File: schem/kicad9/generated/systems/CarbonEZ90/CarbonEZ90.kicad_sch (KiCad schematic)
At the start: 0 parts

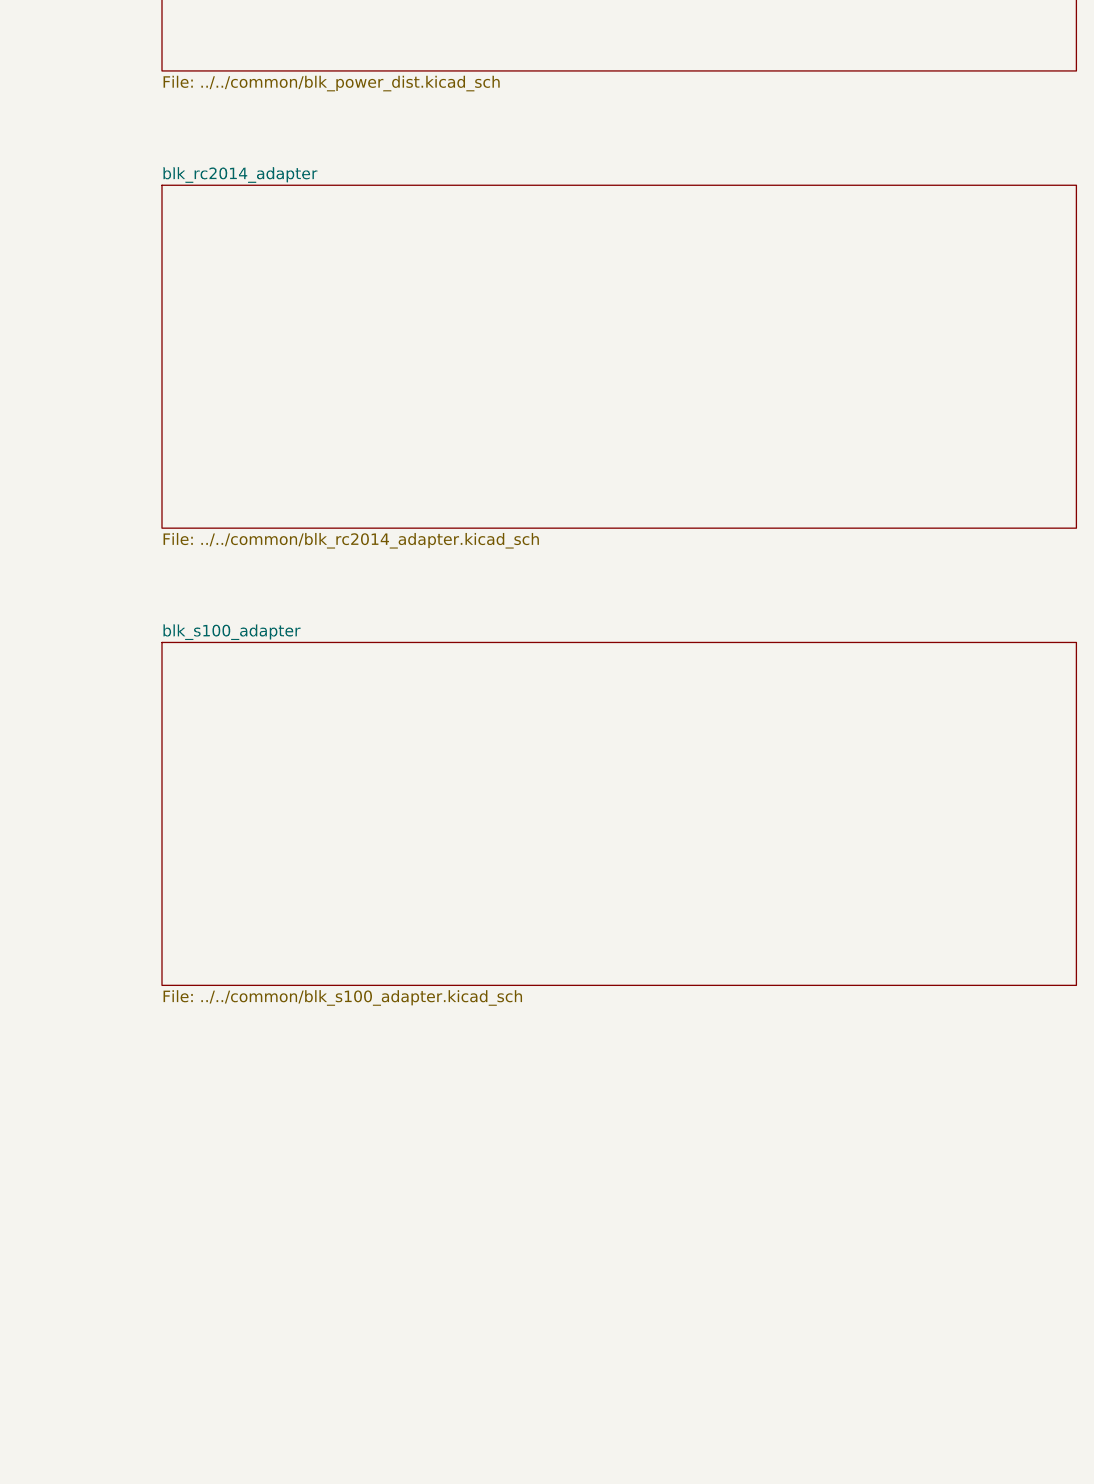
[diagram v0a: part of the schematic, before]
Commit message: kicad: add carbon block symbol library + docs + regen scripts
Detailed description:
- What was implemented: added schem/kicad9/libs/carbon_blocks.kicad_sym placeholder symbols, schem/kicad9/docs/USAGE.md, and scripts/gen_kicad.ps1 plus scripts/gen_kicad.sh; generator now embeds and uses carbon_blocks symbols in generated common block sheets and adds a JTAG/UART common block to system tops.
- Why it exists: keeps the generated hierarchy self-contained and makes regeneration repeatable while reserving a clear path to later map blocks to real parts.
- Architectural assumptions: generator overwrites only schem/kicad9/generated/; carbon_blocks symbols are placeholders (no pin-level mapping in v1); common blocks are represented as simple symbols inside common subsheets.
- How to run it: scripts/gen_kicad.ps1 or scripts/gen_kicad.sh (or python tools/kicadgen/src/kicadgen.py).
- What is NOT implemented yet: automatic mapping to specific 74ACT parts and real footprints, detailed per-net wiring between blocks, and deeper parsing of hdl/spec YAML beyond the mapping specs.
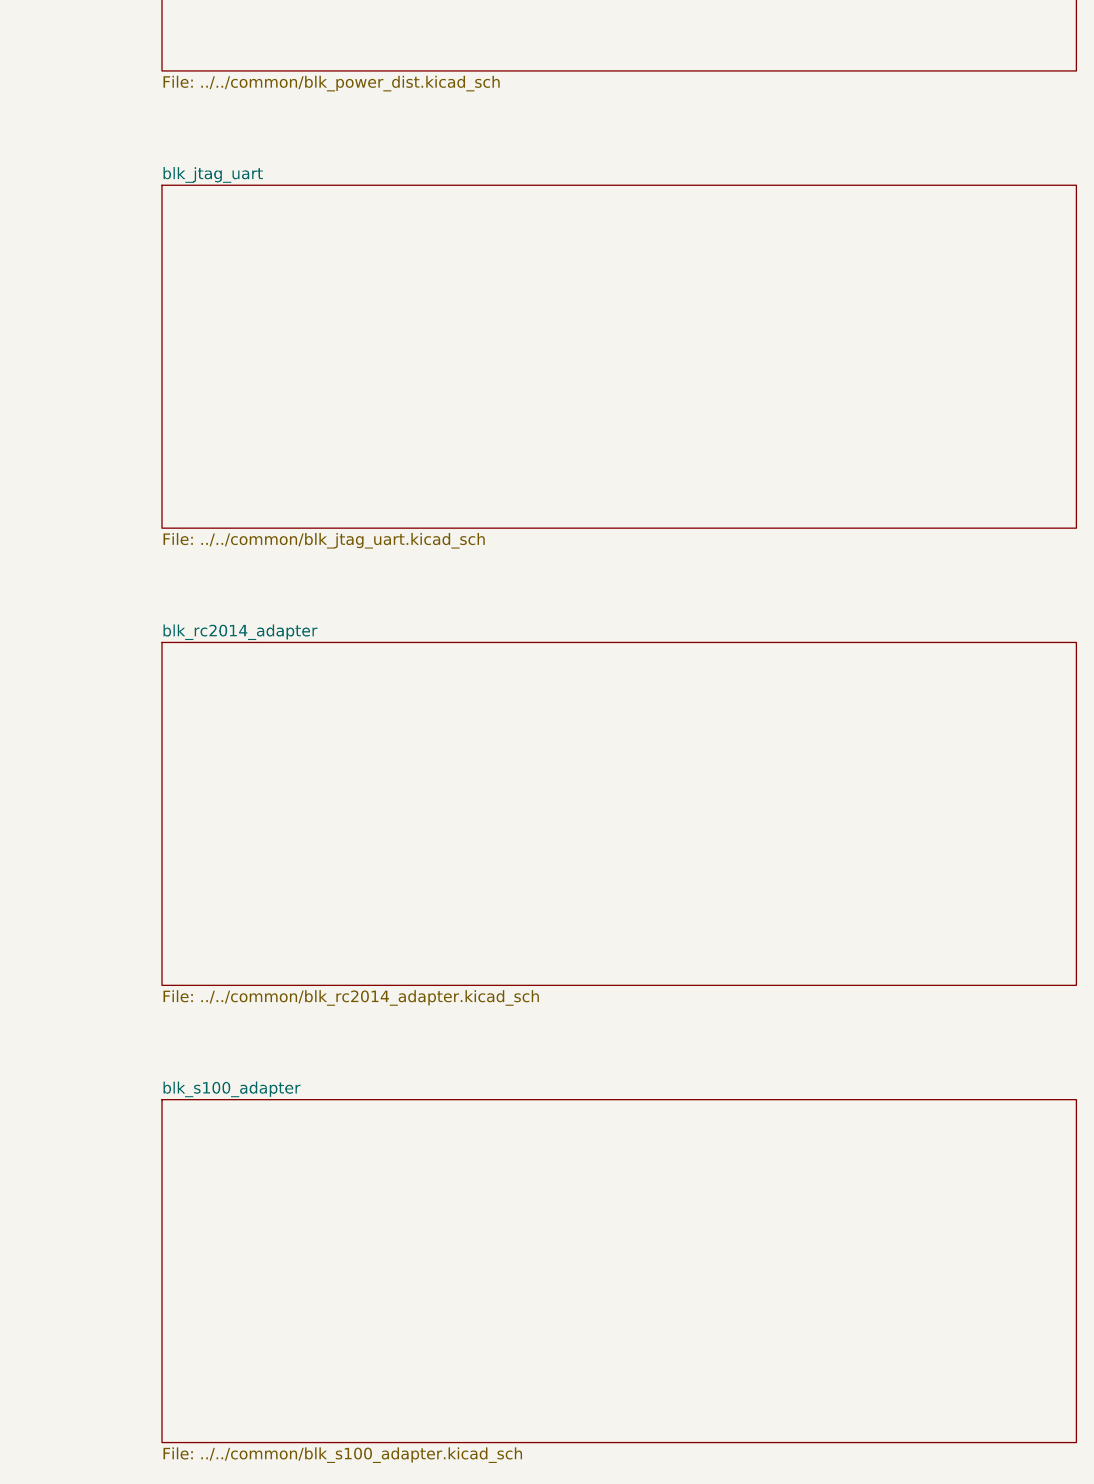
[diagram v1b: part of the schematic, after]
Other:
- added sheet blk_jtag_uart (../../common/blk_jtag_uart.kicad_sch)
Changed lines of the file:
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@@
 		(property
 			"Sheetname"
-			"blk_rc2014_adapter"
+			"blk_jtag_uart"
 			(at
 				139.7
@@
 		(property
 			"Sheetfile"
-			"../../common/blk_rc2014_adapter.kicad_sch"
+			"../../common/blk_jtag_uart.kicad_sch"
 			(at
 				139.7
@@
 		(property
 			"Sheetname"
-			"blk_s100_adapter"
+			"blk_rc2014_adapter"
 			(at
 				139.7
@@
 		(property
 			"Sheetfile"
-			"../../common/blk_s100_adapter.kicad_sch"
+			"../../common/blk_rc2014_adapter.kicad_sch"
 			(at
 				139.7
@@
 				)
 			)
+		)
+	)
+	(sheet
+		(at 139.7 345.44)
+		(size 101.6 38.1)
+		(exclude_from_sim no)
+		(in_bom yes)
+		(on_board yes)
+		(dnp no)
+		(stroke
+			(width 0)
+			(type solid)
+		)
+		(fill
+			(color
+				0
+				0
+				0
+				0
+			)
+		)
+		(property
+			"Sheetname"
+			"blk_s100_adapter"
+			(at
+				139.7
+				344.17
+				0
+			)
+			(effects
+				(font
+					(size 1.27 1.27)
+				)
+				(justify left)
+			)
+		)
+		(property
+			"Sheetfile"
+			"../../common/blk_s100_adapter.kicad_sch"
+			(at
+				139.7
+				384.81
+				0
+			)
+			(effects
+				(font
+					(size 1.27 1.27)
+				)
+				(justify left)
+			)
+		)
+		(instances
+			(project
+				"system_CarbonEZ90"
+				(path
+					"/17675ba5-bcbf-5d72-8a1b-6c49952c9687"
+					(page "12")
+				)
+			)
